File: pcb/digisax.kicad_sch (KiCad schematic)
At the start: 53 parts, among them SW1 RotaryEncoder_Switch, U1 ER_OLEDM0.91_1x-I2C, U2 MPXV7007, U3 MCP3221, U4 TLV320DAC3100_breakout, U5 ESP32-S3

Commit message: added all symbols :D
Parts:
- BT1: footprint (none) -> digisax_stuff:5V0_terminal
- C1: value C470pF -> 470pF; footprint (none) -> Capacitor_THT:C_Disc_D4.7mm_W2.5mm_P5.00mm
- C2, C3: footprint (none) -> Capacitor_THT:C_Disc_D4.7mm_W2.5mm_P5.00mm
- C4: footprint (none) -> Capacitor_THT:CP_Radial_D6.3mm_P2.50mm
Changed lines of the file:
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@@
 			)
 		)
-		(property "Footprint" ""
+		(property "Footprint" "Capacitor_THT:C_Disc_D4.7mm_W2.5mm_P5.00mm"
 			(at 133.0452 151.13 0)
 			(hide yes)
@@
 			)
 		)
-		(property "Value" "C470pF"
+		(property "Value" "470pF"
 			(at 132.08 171.4499 0)
 			(show_name no)
@@
 			)
 		)
-		(property "Footprint" ""
+		(property "Footprint" "Capacitor_THT:C_Disc_D4.7mm_W2.5mm_P5.00mm"
 			(at 129.2352 173.99 0)
 			(hide yes)
@@
 			)
 		)
-		(property "Footprint" ""
+		(property "Footprint" "digisax_stuff:5V0_terminal"
 			(at 187.96 97.536 90)
 			(hide yes)
@@
 			)
 		)
-		(property "Footprint" ""
+		(property "Footprint" "Capacitor_THT:C_Disc_D4.7mm_W2.5mm_P5.00mm"
 			(at 188.9252 74.93 0)
 			(hide yes)
@@
 			)
 		)
-		(property "Footprint" ""
+		(property "Footprint" "Capacitor_THT:CP_Radial_D6.3mm_P2.50mm"
 			(at 202.8952 102.87 0)
 			(hide yes)

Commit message: new switch models.. yeah
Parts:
- key_Bflat1: renamed from key_BF1; footprint Button_Switch_Keyboard:SW_Cherry_MX_1.00u_PCB -> digisax_stuff:slim_switch
- key_C1, key_L1, key_L2, key_L3, key_LB1, key_R1, key_R2, key_R3, key_RS1, key_RS2, key_RS3: footprint Button_Switch_Keyboard:SW_Cherry_MX_1.00u_PCB -> digisax_stuff:slim_switch
- key_Csharp1: renamed from key_CS1; footprint Button_Switch_Keyboard:SW_Cherry_MX_1.00u_PCB -> digisax_stuff:slim_switch
- key_Dsharp1: renamed from key_DS1; footprint Button_Switch_Keyboard:SW_Cherry_MX_1.00u_PCB -> digisax_stuff:slim_switch
- key_Gsharp1: renamed from key_GS1; footprint Button_Switch_Keyboard:SW_Cherry_MX_1.00u_PCB -> digisax_stuff:slim_switch
- key_LBflat1: renamed from key_LBF1; footprint Button_Switch_Keyboard:SW_Cherry_MX_1.00u_PCB -> digisax_stuff:slim_switch
- key_Lside1: renamed from key_LS1; footprint Button_Switch_Keyboard:SW_Cherry_MX_1.00u_PCB -> digisax_stuff:slim_switch
- key_Lside2: renamed from key_LS2; footprint Button_Switch_Keyboard:SW_Cherry_MX_1.00u_PCB -> digisax_stuff:slim_switch
- key_Lside3: renamed from key_LS3; footprint Button_Switch_Keyboard:SW_Cherry_MX_1.00u_PCB -> digisax_stuff:slim_switch
- key_fork1: renamed from key_FORK1; footprint Button_Switch_Keyboard:SW_Cherry_MX_1.00u_PCB -> digisax_stuff:slim_switch
- key_octave1: renamed from key_8VE1; footprint Button_Switch_Keyboard:SW_Cherry_MX_1.00u_PCB -> digisax_stuff:slim_switch
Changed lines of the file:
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@@
 			)
 		)
-		(property "Footprint" "Button_Switch_Keyboard:SW_Cherry_MX_1.00u_PCB"
+		(property "Footprint" "digisax_stuff:slim_switch"
 			(at 74.93 99.06 0)
 			(hide yes)
@@
 		(dnp no)
 		(fields_autoplaced yes)
-		(property "Reference" "key_LS3"
+		(property "Reference" "key_Lside3"
 			(at 105.41 66.04 0)
 			(show_name no)
@@
 			)
 		)
-		(property "Footprint" "Button_Switch_Keyboard:SW_Cherry_MX_1.00u_PCB"
+		(property "Footprint" "digisax_stuff:slim_switch"
 			(at 105.41 68.58 0)
 			(hide yes)
@@
 			(project "digisax"
 				(path "/eb5dc4d3-8e2b-4a19-9d6b-e55e1d276974"
-					(reference "key_LS3")
+					(reference "key_Lside3")
 					(unit 1)
 				)
@@
 		(dnp no)
 		(fields_autoplaced yes)
-		(property "Reference" "key_DS1"
+		(property "Reference" "key_Dsharp1"
 			(at 45.72 86.36 0)
 			(show_name no)
@@
 			)
 		)
-		(property "Footprint" "Button_Switch_Keyboard:SW_Cherry_MX_1.00u_PCB"
+		(property "Footprint" "digisax_stuff:slim_switch"
 			(at 45.72 88.9 0)
 			(hide yes)
@@
 			(project "digisax"
 				(path "/eb5dc4d3-8e2b-4a19-9d6b-e55e1d276974"
-					(reference "key_DS1")
+					(reference "key_Dsharp1")
 					(unit 1)
 				)
@@
 			)
 		)
-		(property "Footprint" "Button_Switch_Keyboard:SW_Cherry_MX_1.00u_PCB"
+		(property "Footprint" "digisax_stuff:slim_switch"
 			(at 45.72 99.06 0)
 			(hide yes)
@@
 			)
 		)
-		(property "Footprint" "Button_Switch_Keyboard:SW_Cherry_MX_1.00u_PCB"
+		(property "Footprint" "digisax_stuff:slim_switch"
 			(at 74.93 78.74 0)
 			(hide yes)
@@
 		(dnp no)
 		(fields_autoplaced yes)
-		(property "Reference" "key_LBF1"
+		(property "Reference" "key_LBflat1"
 			(at 105.41 106.68 0)
 			(show_name no)
@@
 			)
 		)
-		(property "Footprint" "Button_Switch_Keyboard:SW_Cherry_MX_1.00u_PCB"
+		(property "Footprint" "digisax_stuff:slim_switch"
 			(at 105.41 109.22 0)
 			(hide yes)
@@
 			(project "digisax"
 				(path "/eb5dc4d3-8e2b-4a19-9d6b-e55e1d276974"
-					(reference "key_LBF1")
+					(reference "key_LBflat1")
 					(unit 1)
 				)
@@
 		(dnp no)
 		(fields_autoplaced yes)
-		(property "Reference" "key_LS2"
+		(property "Reference" "key_Lside2"
 			(at 105.41 55.88 0)
 			(show_name no)
@@
 			)
 		)
-		(property "Footprint" "Button_Switch_Keyboard:SW_Cherry_MX_1.00u_PCB"
+		(property "Footprint" "digisax_stuff:slim_switch"
 			(at 105.41 58.42 0)
 			(hide yes)
@@
 			(project "digisax"
 				(path "/eb5dc4d3-8e2b-4a19-9d6b-e55e1d276974"
-					(reference "key_LS2")
+					(reference "key_Lside2")
 					(unit 1)
 				)
@@
 			)
 		)
-		(property "Footprint" "Button_Switch_Keyboard:SW_Cherry_MX_1.00u_PCB"
+		(property "Footprint" "digisax_stuff:slim_switch"
 			(at 45.72 68.58 0)
 			(hide yes)
@@
 			)
 		)
-		(property "Footprint" "Button_Switch_Keyboard:SW_Cherry_MX_1.00u_PCB"
+		(property "Footprint" "digisax_stuff:slim_switch"
 			(at 74.93 68.58 0)
 			(hide yes)
@@
 		(dnp no)
 		(fields_autoplaced yes)
-		(property "Reference" "key_FORK1"
+		(property "Reference" "key_fork1"
 			(at 45.72 106.68 0)
 			(show_name no)
@@
 			)
 		)
-		(property "Footprint" "Button_Switch_Keyboard:SW_Cherry_MX_1.00u_PCB"
+		(property "Footprint" "digisax_stuff:slim_switch"
 			(at 45.72 109.22 0)
 			(hide yes)
@@
 			(project "digisax"
 				(path "/eb5dc4d3-8e2b-4a19-9d6b-e55e1d276974"
-					(reference "key_FORK1")
+					(reference "key_fork1")
 					(unit 1)
 				)
@@
 			)
 		)
-		(property "Footprint" "Button_Switch_Keyboard:SW_Cherry_MX_1.00u_PCB"
+		(property "Footprint" "digisax_stuff:slim_switch"
 			(at 74.93 48.26 0)
 			(hide yes)
@@
 		(dnp no)
 		(fields_autoplaced yes)
-		(property "Reference" "key_8VE1"
+		(property "Reference" "key_octave1"
 			(at 45.72 45.72 0)
 			(show_name no)
@@
 			)
 		)
-		(property "Footprint" "Button_Switch_Keyboard:SW_Cherry_MX_1.00u_PCB"
+		(property "Footprint" "digisax_stuff:slim_switch"
 			(at 45.72 48.26 0)
 			(hide yes)
@@
 			(project "digisax"
 				(path "/eb5dc4d3-8e2b-4a19-9d6b-e55e1d276974"
-					(reference "key_8VE1")
+					(reference "key_octave1")
 					(unit 1)
 				)
@@
 		(dnp no)
 		(fields_autoplaced yes)
-		(property "Reference" "key_LS1"
+		(property "Reference" "key_Lside1"
 			(at 105.41 45.72 0)
 			(show_name no)
@@
 			)
 		)
-		(property "Footprint" "Button_Switch_Keyboard:SW_Cherry_MX_1.00u_PCB"
+		(property "Footprint" "digisax_stuff:slim_switch"
 			(at 105.41 48.26 0)
 			(hide yes)
@@
 			(project "digisax"
 				(path "/eb5dc4d3-8e2b-4a19-9d6b-e55e1d276974"
-					(reference "key_LS1")
+					(reference "key_Lside1")
 					(unit 1)
 				)
@@
 		(dnp no)
 		(fields_autoplaced yes)
-		(property "Reference" "key_BF1"
+		(property "Reference" "key_Bflat1"
 			(at 74.93 55.88 0)
 			(show_name no)
@@
 			)
 		)
-		(property "Footprint" "Button_Switch_Keyboard:SW_Cherry_MX_1.00u_PCB"
+		(property "Footprint" "digisax_stuff:slim_switch"
 			(at 74.93 58.42 0)
 			(hide yes)
@@
 			(project "digisax"
 				(path "/eb5dc4d3-8e2b-4a19-9d6b-e55e1d276974"
-					(reference "key_BF1")
+					(reference "key_Bflat1")
 					(unit 1)
 				)
@@
 			)
 		)
-		(property "Footprint" "Button_Switch_Keyboard:SW_Cherry_MX_1.00u_PCB"
+		(property "Footprint" "digisax_stuff:slim_switch"
 			(at 74.93 88.9 0)
 			(hide yes)
@@
 		(dnp no)
 		(fields_autoplaced yes)
-		(property "Reference" "key_GS1"
+		(property "Reference" "key_Gsharp1"
 			(at 105.41 76.2 0)
 			(show_name no)
@@
 			)
 		)
-		(property "Footprint" "Button_Switch_Keyboard:SW_Cherry_MX_1.00u_PCB"
+		(property "Footprint" "digisax_stuff:slim_switch"
 			(at 105.41 78.74 0)
 			(hide yes)
@@
 			(project "digisax"
 				(path "/eb5dc4d3-8e2b-4a19-9d6b-e55e1d276974"
-					(reference "key_GS1")
+					(reference "key_Gsharp1")
 					(unit 1)
 				)
@@
 		(dnp no)
 		(fields_autoplaced yes)
-		(property "Reference" "key_CS1"
+		(property "Reference" "key_Csharp1"
 			(at 105.41 86.36 0)
 			(show_name no)
@@
 			)
 		)
-		(property "Footprint" "Button_Switch_Keyboard:SW_Cherry_MX_1.00u_PCB"
+		(property "Footprint" "digisax_stuff:slim_switch"
 			(at 105.41 88.9 0)
 			(hide yes)
@@
 			(project "digisax"
 				(path "/eb5dc4d3-8e2b-4a19-9d6b-e55e1d276974"
-					(reference "key_CS1")
+					(reference "key_Csharp1")
 					(unit 1)
 				)
@@
 			)
 		)
-		(property "Footprint" "Button_Switch_Keyboard:SW_Cherry_MX_1.00u_PCB"
+		(property "Footprint" "digisax_stuff:slim_switch"
 			(at 45.72 58.42 0)
 			(hide yes)
@@
 			)
 		)
-		(property "Footprint" "Button_Switch_Keyboard:SW_Cherry_MX_1.00u_PCB"
+		(property "Footprint" "digisax_stuff:slim_switch"
 			(at 105.41 99.06 0)
 			(hide yes)
@@
 			)
 		)
-		(property "Footprint" "Button_Switch_Keyboard:SW_Cherry_MX_1.00u_PCB"
+		(property "Footprint" "digisax_stuff:slim_switch"
 			(at 45.72 78.74 0)
 			(hide yes)
@@
 			)
 		)
-		(property "Footprint" "Button_Switch_Keyboard:SW_Cherry_MX_1.00u_PCB"
+		(property "Footprint" "digisax_stuff:slim_switch"
 			(at 74.93 109.22 0)
 			(hide yes)

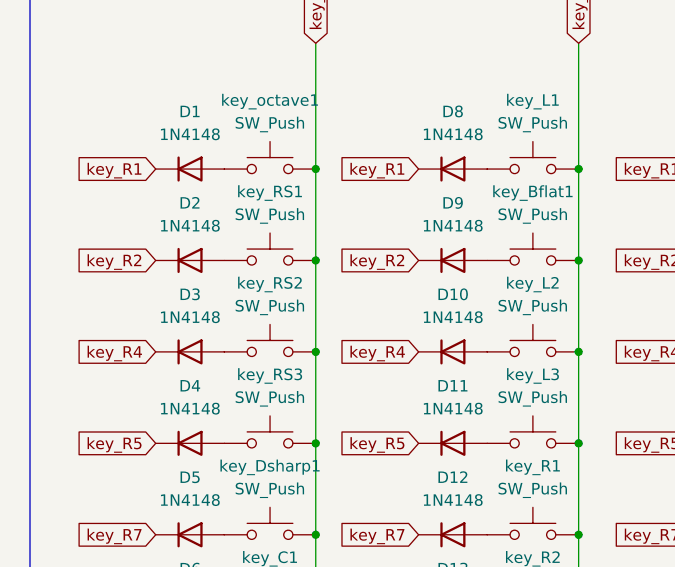
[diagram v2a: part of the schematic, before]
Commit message: switch placement according to irl sax
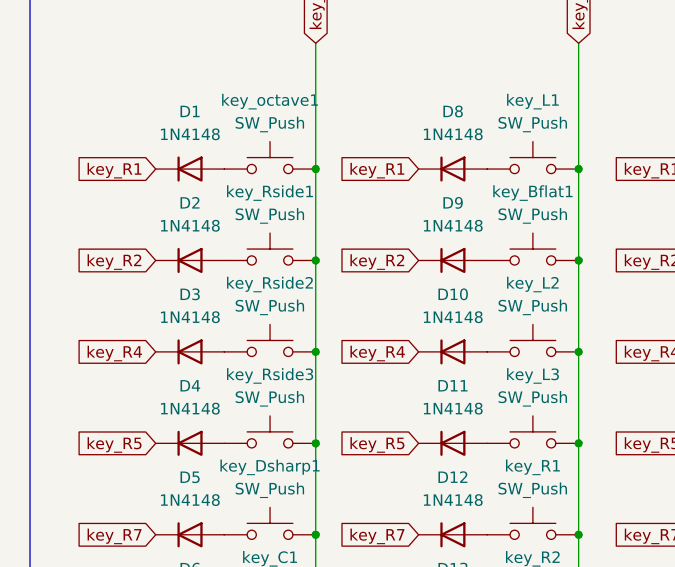
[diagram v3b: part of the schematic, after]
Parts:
- renumbered key_RS1 to key_Rside1, key_RS2 to key_Rside2, key_RS3 to key_Rside3
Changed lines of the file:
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@@
 		(dnp no)
 		(fields_autoplaced yes)
-		(property "Reference" "key_RS2"
+		(property "Reference" "key_Rside2"
 			(at 45.72 66.04 0)
 			(show_name no)
@@
 			(project "digisax"
 				(path "/eb5dc4d3-8e2b-4a19-9d6b-e55e1d276974"
-					(reference "key_RS2")
+					(reference "key_Rside2")
 					(unit 1)
 				)
@@
 		(dnp no)
 		(fields_autoplaced yes)
-		(property "Reference" "key_RS1"
+		(property "Reference" "key_Rside1"
 			(at 45.72 55.88 0)
 			(show_name no)
@@
 			(project "digisax"
 				(path "/eb5dc4d3-8e2b-4a19-9d6b-e55e1d276974"
-					(reference "key_RS1")
+					(reference "key_Rside1")
 					(unit 1)
 				)
@@
 		(dnp no)
 		(fields_autoplaced yes)
-		(property "Reference" "key_RS3"
+		(property "Reference" "key_Rside3"
 			(at 45.72 76.2 0)
 			(show_name no)
@@
 			(project "digisax"
 				(path "/eb5dc4d3-8e2b-4a19-9d6b-e55e1d276974"
-					(reference "key_RS3")
+					(reference "key_Rside3")
 					(unit 1)
 				)

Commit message: added headers to schem
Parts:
- added J1, J2, J5, J6: Conn_01x04_Pin, symbol Connector:Conn_01x04_Pin
- added J3, J4: Conn_01x05_Pin, symbol Connector:Conn_01x05_Pin
- added J7, J8: Conn_01x03_Pin, symbol Connector:Conn_01x03_Pin
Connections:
- net key_C1: no longer key_C1.2, key_Dsharp1.2, key_Rside1.2, key_Rside2.2, key_Rside3.2, key_fork1.2, key_octave1.2
- net key_C2: no longer key_Bflat1.2, key_L1.2, key_L2.2, key_L3.2, key_R1.2, key_R2.2, key_R3.2
- net key_C3: no longer key_Csharp1.2, key_Gsharp1.2, key_LB1.2, key_LBflat1.2, key_Lside1.2, key_Lside2.2, key_Lside3.2
- net key_R1: no longer D1.1 (K), D15.1 (K), D8.1 (K)
- net key_R2: no longer D16.1 (K), D2.1 (K), D9.1 (K)
- net key_R4: no longer D10.1 (K), D17.1 (K), D3.1 (K)
- net key_R5: no longer D11.1 (K), D18.1 (K), D4.1 (K)
- net key_R7: no longer D12.1 (K), D19.1 (K), D5.1 (K)
- net key_R8: no longer D13.1 (K), D20.1 (K), D6.1 (K)
- net key_R9: no longer D14.1 (K), D21.1 (K), D7.1 (K)
- new net: J1.4 (Pin_4), key_Lside1.2, key_Lside2.2, key_Lside3.2
- new net: J7.3 (Pin_3), key_C1.2, key_Dsharp1.2
- new net: D6.1 (K), J7.2 (Pin_2)
- new net: D15.1 (K), J1.1 (Pin_1)
- new net: D19.1 (K), J3.2 (Pin_2)
- new net: D4.1 (K), J5.3 (Pin_3)
- new net: J3.5 (Pin_5), key_Csharp1.2, key_Gsharp1.2, key_LB1.2, key_LBflat1.2
- new net: D2.1 (K), J5.1 (Pin_1)
- new net: J5.4 (Pin_4), key_Rside1.2, key_Rside2.2, key_Rside3.2
- new net: D3.1 (K), J5.2 (Pin_2)
- new net: D16.1 (K), J1.2 (Pin_2)
- new net: D18.1 (K), J3.1 (Pin_1)
- new net: D5.1 (K), J7.1 (Pin_1)
- new net: D17.1 (K), J1.3 (Pin_3)
- new net: D20.1 (K), J3.3 (Pin_3)
- new net: D21.1 (K), J3.4 (Pin_4)
- new net key_col1: J6.4 (Pin_4), J8.3 (Pin_3), key_fork1.2, key_octave1.2
- new net key_col2: key_Bflat1.2, key_L1.2, key_L2.2, key_L3.2, key_R1.2, key_R2.2, key_R3.2
- new net key_col3: J2.4 (Pin_4), J4.5 (Pin_5)
- new net key_row1: D1.1 (K), D8.1 (K), J2.1 (Pin_1)
- new net key_row2: D9.1 (K), J2.2 (Pin_2), J6.1 (Pin_1)
- new net key_row3: D10.1 (K), J2.3 (Pin_3), J6.2 (Pin_2)
- new net key_row4: D11.1 (K), J4.1 (Pin_1), J6.3 (Pin_3)
- new net key_row5: D12.1 (K), J4.2 (Pin_2), J8.1 (Pin_1)
- new net key_row6: D13.1 (K), J4.3 (Pin_3), J8.2 (Pin_2)
- new net key_row7: D14.1 (K), D7.1 (K), J4.4 (Pin_4)
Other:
- moved on the sheet: BT1, C1, C2, C3, C4, D1, D10, D11, D12, D13, D14, D15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

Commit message: more kcal burnt on pcb
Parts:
- J1, J2, J5, J6: footprint (none) -> digisax_stuff:pad_1x4
- J3, J4: footprint (none) -> digisax_stuff:pad_1x5
- J7, J8: footprint (none) -> digisax_stuff:pad_1x3
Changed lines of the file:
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@@
 			)
 		)
-		(property "Footprint" ""
+		(property "Footprint" "digisax_stuff:pad_1x4"
 			(at 24.13 90.17 0)
 			(hide yes)
@@
 			)
 		)
-		(property "Footprint" ""
+		(property "Footprint" "digisax_stuff:pad_1x3"
 			(at 24.13 118.11 0)
 			(hide yes)
@@
 			)
 		)
-		(property "Footprint" ""
+		(property "Footprint" "digisax_stuff:pad_1x4"
 			(at 52.07 90.17 0)
 			(hide yes)
@@
 			)
 		)
-		(property "Footprint" ""
+		(property "Footprint" "digisax_stuff:pad_1x5"
 			(at 137.16 93.98 0)
 			(hide yes)
@@
 			)
 		)
-		(property "Footprint" ""
+		(property "Footprint" "digisax_stuff:pad_1x3"
 			(at 52.07 118.11 0)
 			(hide yes)
@@
 			)
 		)
-		(property "Footprint" ""
+		(property "Footprint" "digisax_stuff:pad_1x4"
 			(at 166.37 50.8 0)
 			(hide yes)
@@
 			)
 		)
-		(property "Footprint" ""
+		(property "Footprint" "digisax_stuff:pad_1x5"
 			(at 163.83 93.98 0)
 			(hide yes)
@@
 			)
 		)
-		(property "Footprint" ""
+		(property "Footprint" "digisax_stuff:pad_1x4"
 			(at 137.16 50.8 0)
 			(hide yes)

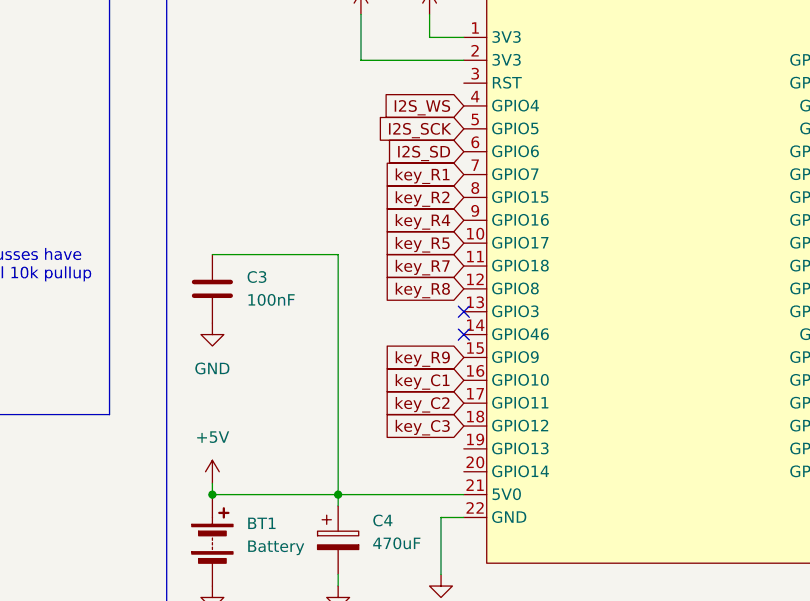
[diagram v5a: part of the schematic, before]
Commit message: fixed schematic labels
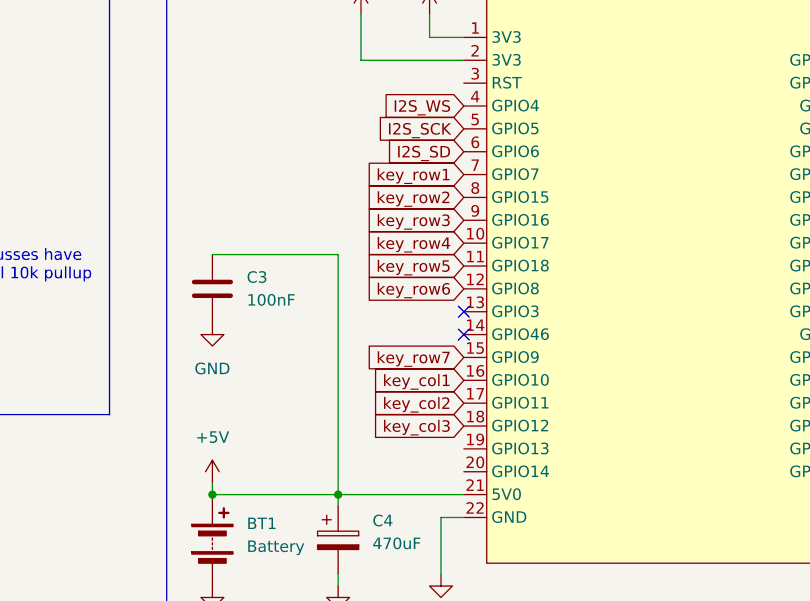
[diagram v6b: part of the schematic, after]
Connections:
- net key_C1 is gone; now on net key_col1: U5.16 (GPIO10)
- net key_C2 is gone; now on net key_col2: U5.17 (GPIO11)
- net key_C3 is gone; now on net key_col3: U5.18 (GPIO12)
- net key_R1 is gone; now on net key_row1: U5.7 (GPIO7)
- net key_R2 is gone; now on net key_row2: U5.8 (GPIO15)
- net key_R4 is gone; now on net key_row3: U5.9 (GPIO16)
- net key_R5 is gone; now on net key_row4: U5.10 (GPIO17)
- net key_R7 is gone; now on net key_row5: U5.11 (GPIO18)
- net key_R8 is gone; now on net key_row6: U5.12 (GPIO8)
- net key_R9 is gone; now on net key_row7: U5.15 (GPIO9)

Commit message: added barrel jack, sketched board outline
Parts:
- added J9: Barrel_Jack, Connector_BarrelJack:BarrelJack_Horizontal, symbol Connector:Barrel_Jack
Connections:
- net +5V: now also J9.1
- net GND: now also J9.2

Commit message: had a go at routing
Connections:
- net I2C_SCL: now also U5.31 (GPIO39)
- net I2C_SDA: now also U5.30 (GPIO40)
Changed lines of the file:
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@@
+		)
+	)
+	(global_label "I2C_SDA"
+		(shape input)
+		(at 370.84 81.28 0)
+		(fields_autoplaced yes)
+		(effects
+			(font
+				(size 1.27 1.27)
+			)
+			(justify left)
+		)
+		(property "Intersheetrefs" "${INTERSHEET_REFS}"
+			(at 381.4452 81.28 0)
+			(hide yes)
+			(show_name no)
+			(do_not_autoplace no)
+			(effects
+				(font
+					(size 1.27 1.27)
+				)
+				(justify left)
+			)
 		)
 	)
@@
 			)
 		)
+	)
+	(global_label "I2C_SCL"
+		(shape input)
+		(at 370.84 83.82 0)
+		(fields_autoplaced yes)
+		(effects
+			(font
+				(size 1.27 1.27)
+			)
+			(justify left)
+		)
+		(property "Intersheetrefs" "${INTERSHEET_REFS}"
+			(at 381.3847 83.82 0)
+			(hide yes)
+			(show_name no)
+			(do_not_autoplace no)
+			(effects
+				(font
+					(size 1.27 1.27)
+				)
+				(justify left)
+			)
+		)
